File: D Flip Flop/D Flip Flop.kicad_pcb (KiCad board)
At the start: 2 copper layers, 41 parts, among them J101 USB_A, SW101 SW_Push, SW102 SW_Push, SW103 SW_Push, SW201 SW_Push, U201 LM555xM, U301 74HC00, U401 74HC00, U501 74HC00, U601 74HC00, U701 74HC00, U801 74HC00

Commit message: Rough layout
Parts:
- moved U501 140.6 mm to (90.2, 104.1)
- moved C501 140.5 mm to (86.4, 102.9)
- moved D601 138.2 mm to (123.2, 128.3)
- moved U601 138.2 mm to (90.2, 132.1)
- moved C601 138.2 mm to (86.4, 130.8)
- moved D501 137.8 mm to (130.8, 100.3)
- moved R501 137.1 mm to (110.5, 104.1), turned to 90 degrees
- moved R601 134.8 mm to (110.5, 132.1), turned to 90 degrees
- moved R801 132.8 mm to (171.4, 104.1), turned to 90 degrees
- moved R701 129.0 mm to (171.4, 76.2), turned to 90 degrees
- moved D801 128.2 mm to (189.2, 100.3)
- moved U701 127.0 mm to (151.1, 76.2)
- moved U801 127.0 mm to (151.1, 104.1)
- moved C801 127.0 mm to (147.3, 102.9)
- moved C701 127.0 mm to (147.3, 74.9)
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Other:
- board outline added: 203.2 x 147.3 mm
- board text added: "Clock"
- board text added: "Data"
- board text added: "Q"
- board text added: "~{Clear}"
- board text added: "~{Q}"

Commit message: Completed first draft
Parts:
- added H101: MountingHole, MountingHole:MountingHole_2.2mm_M2, F.Cu at (26.7, 20.3)
- added H102: MountingHole, MountingHole:MountingHole_2.2mm_M2, F.Cu at (214.6, 20.3)
- added H103: MountingHole, MountingHole:MountingHole_2.2mm_M2, F.Cu at (26.7, 152.4)
- added H104: MountingHole, MountingHole:MountingHole_2.2mm_M2, F.Cu at (214.6, 152.4)
- moved J101 6.48 mm to (208.0, 130.5)
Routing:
- net /~{CLEAR}: track 0.00 -> 347.4 mm, vias 0 -> 1
- net /NAND 0/C: track 0.00 -> 210.3 mm, vias 0 -> 4
- net /~{PRESET}: track 0.00 -> 191.0 mm, vias 0 -> 1
- net /NAND 0/B: track 0.00 -> 162.7 mm, vias 0 -> 4
- net /NAND 2/OUT: track 0.00 -> 157.6 mm, vias 0 -> 2
- net /CLK: track 0.00 -> 123.2 mm, vias 0 -> 1
- net /~{Q}: track 0.00 -> 107.8 mm, vias 0 -> 1
- net /Q: track 0.00 -> 100.1 mm, vias 0 -> 3
- net /NAND 0/OUT: track 0.00 -> 69.7 mm, vias 0 -> 1
- net /DATA: track 0.00 -> 64.7 mm, vias 0 -> 2
- net Net-(R201-Pad2): track 0.00 -> 41.2 mm
- net Net-(D501-Pad2): track 0.00 -> 21.4 mm
- net Net-(D401-Pad2): track 0.00 -> 21.4 mm
- net Net-(R601-Pad1): track 0.00 -> 20.0 mm
- net Net-(R801-Pad1): track 0.00 -> 20.0 mm
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- added copper zone on B.Cu, net +5V
- added copper zone on F.Cu, net GND
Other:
- board size 203.2 x 147.3 mm -> 200.7 x 144.8 mm
- board text added: "D Flip-Flop"
- board text added: "JLCJLCJLCJLC"
- board text added: "RGE2023"
- board text added: "~{Preset}"
- board text removed: "~{PRESET}"

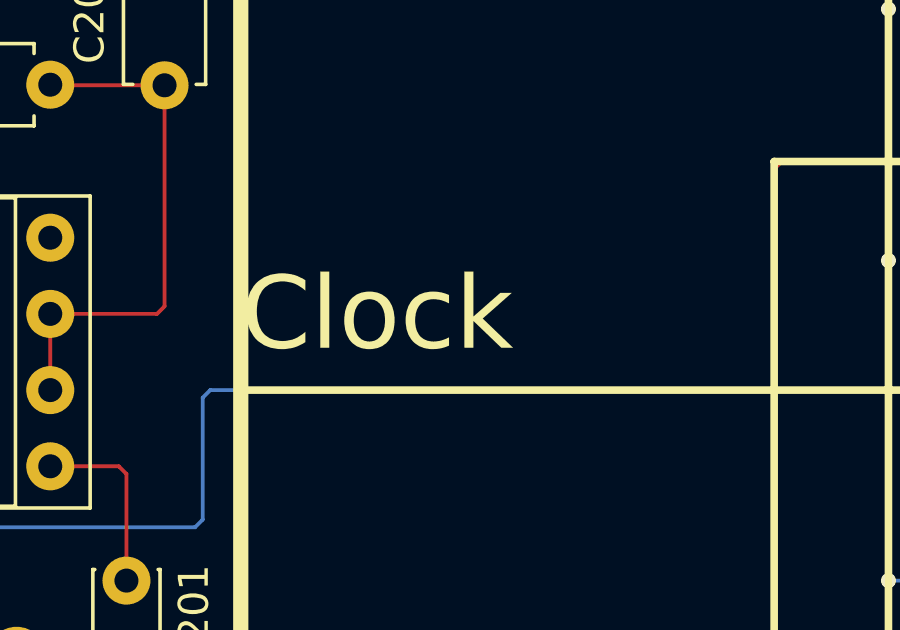
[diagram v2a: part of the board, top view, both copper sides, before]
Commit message: Don't need monostable for clock
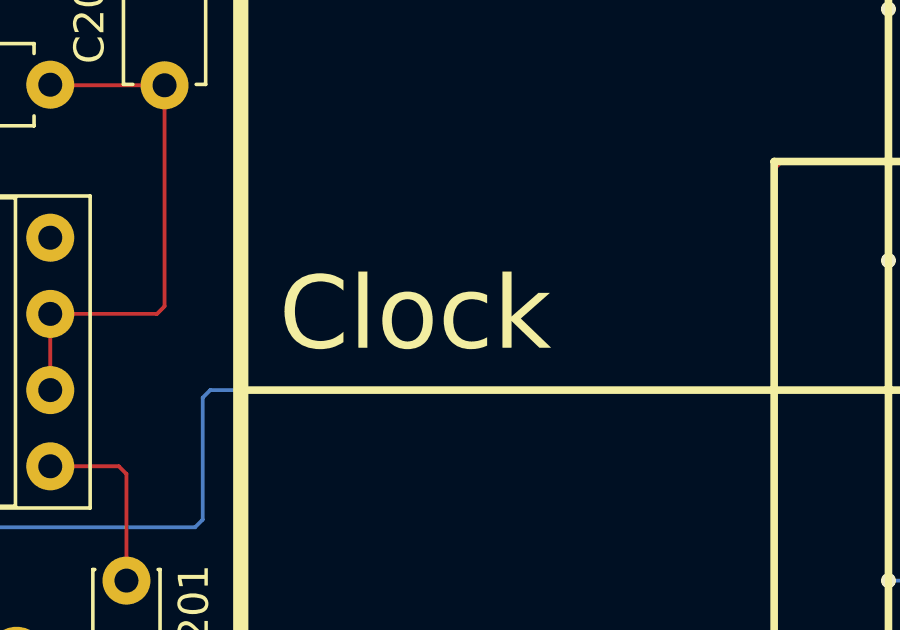
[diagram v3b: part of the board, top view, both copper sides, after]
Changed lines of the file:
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@@
     (effects (font (size 6.5024 6.5024) (thickness 0.8128)) (justify left))
   )
-  (gr_text "Clock" (at 46.99 82.55) (layer "F.SilkS")
+  (gr_text "Clock" (at 48.26 82.55) (layer "F.SilkS")
     (effects (font (size 2.4384 2.4384) (thickness 0.4064)) (justify left))
   )
@@
     (connect_pads (clearance 0.254))
     (min_thickness 0.254) (filled_areas_thickness no)
-    (fill yes (thermal_gap 0.508) (thermal_bridge_width 0.508))
+    (fill (thermal_gap 0.508) (thermal_bridge_width 0.508))
     (polygon
       (pts
@@
     (connect_pads (clearance 0.254))
     (min_thickness 0.254) (filled_areas_thickness no)
-    (fill yes (thermal_gap 0.508) (thermal_bridge_width 0.508))
+    (fill (thermal_gap 0.508) (thermal_bridge_width 0.508))
     (polygon
       (pts

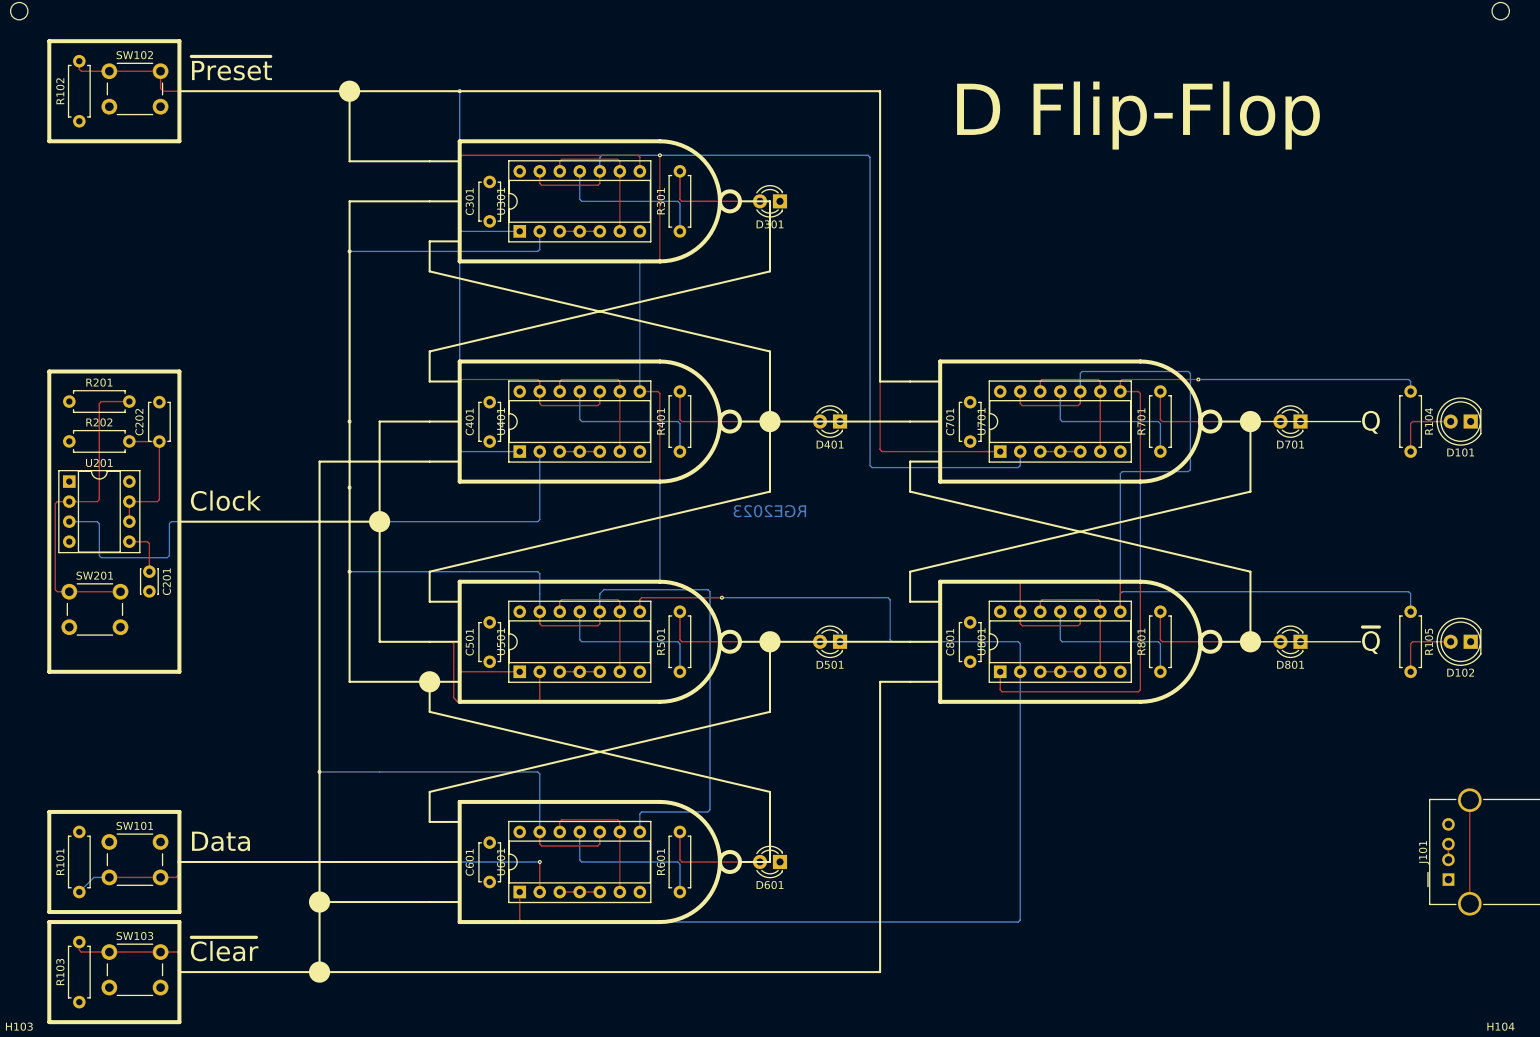
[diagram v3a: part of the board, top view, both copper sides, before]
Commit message: Simplifying board a little
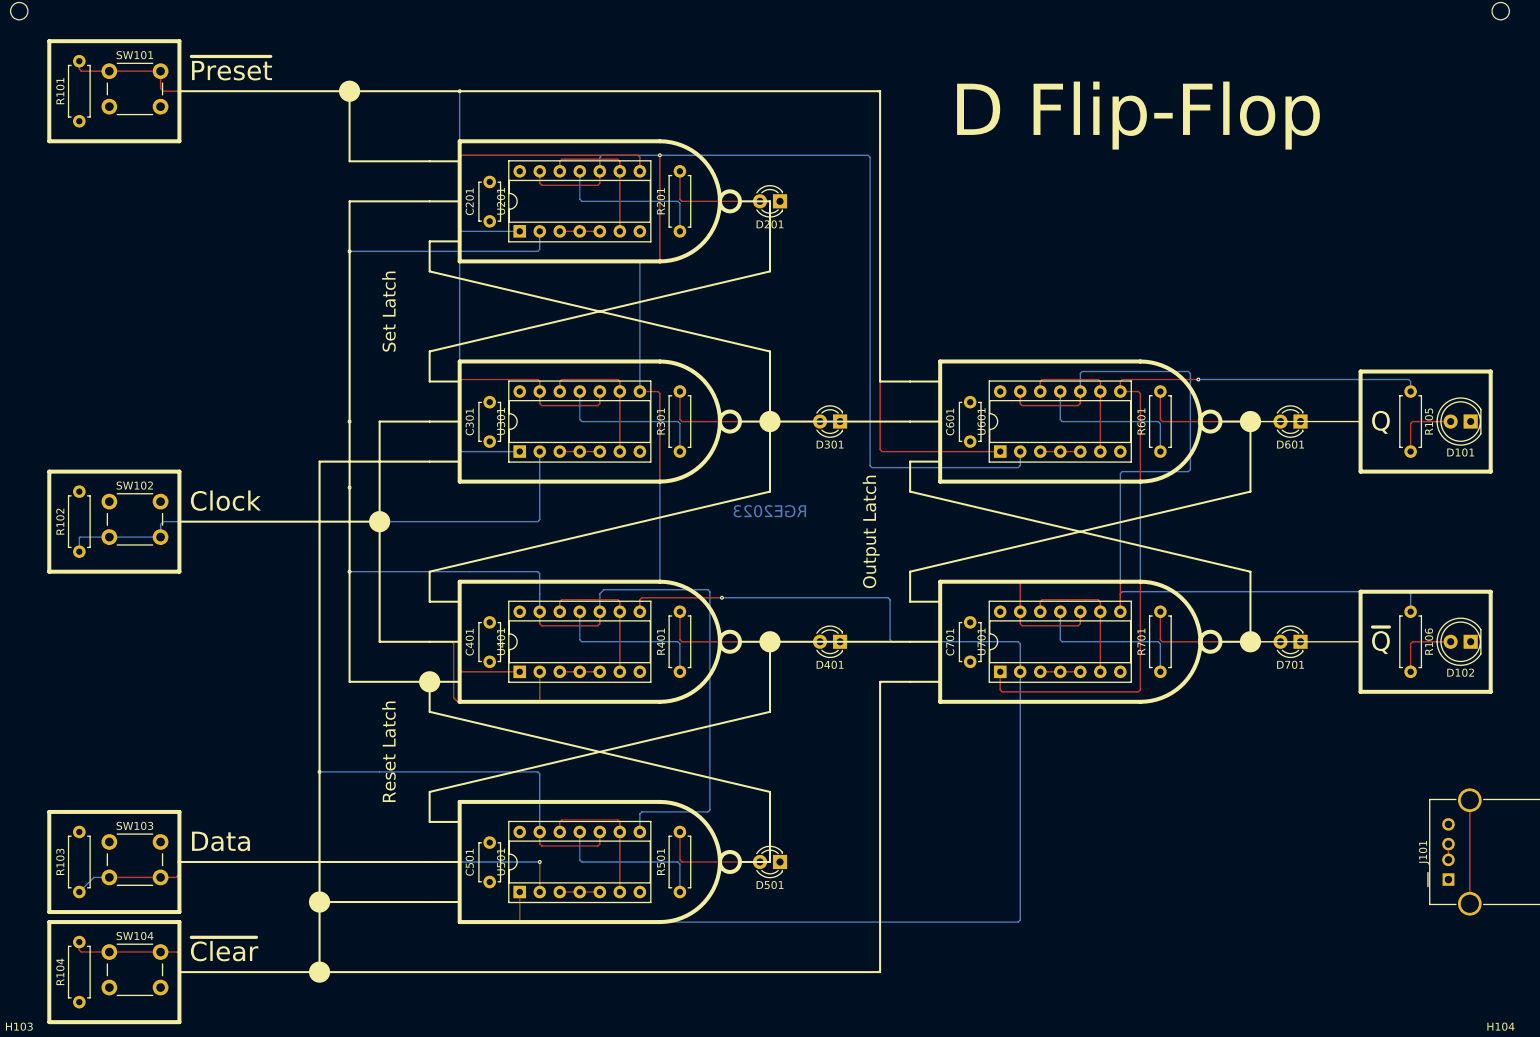
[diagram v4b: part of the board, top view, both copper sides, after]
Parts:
- removed the C201 at (43.2, 91.4)
- removed C202: 0.1u, Capacitor_THT:C_Disc_D4.7mm_W2.5mm_P5.00mm
- removed the R201 at (33.0, 69.8)
- removed R202: 1M, Resistor_THT:R_Axial_DIN0207_L6.3mm_D2.5mm_P7.62mm_Horizontal
- removed SW201: SW_Push, Button_Switch_THT:SW_PUSH_6mm_H4.3mm
- removed the U201 at (33.0, 80.0)
- added R102: 100k, Resistor_THT:R_Axial_DIN0207_L6.3mm_D2.5mm_P7.62mm_Horizontal, F.Cu at (34.3, 88.9)
- added SW102: SW_Push, Button_Switch_THT:SW_PUSH_6mm_H4.3mm, F.Cu at (38.1, 82.5)
- renumbered C301 to C201, C401 to C301, C501 to C401, C601 to C501, C701 to C601, C801 to C701, D301 to D201, D401 to D301, D501 to D401, D601 to D501, D701 to D601, D801 to D701, R102 to R101, R101 to R103, R103 to R104, R104 to R105, R105 to R106, R301 to R201, R401 to R301, R501 to R401, R601 to R501, R701 to R601, R801 to R701, SW102 to SW101, SW101 to SW103, SW103 to SW104, U301 to U201, U401 to U301, U501 to U401, U601 to U501, U701 to U601, U801 to U701
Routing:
- net Net-(R201-Pad2): track 41.2 -> 0.00 mm
- net Net-(C202-Pad1): track 17.6 -> 0.00 mm
- net /CLK: track 123.2 -> 117.0 mm
- net Net-(C201-Pad1): track 6.20 -> 0.00 mm
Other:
- board text added: "Output Latch"
- board text added: "Reset Latch"
- board text added: "Set Latch"
